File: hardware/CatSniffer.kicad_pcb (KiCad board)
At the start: 4 copper layers, 81 x 20 mm, 100 parts, among them J1 Antenna, J3 Conn_01x06_Female, P1 USB_C_Plug_USB2.0, SW1 SW, U1 AP2112K-3.3, U2 RFSW8006QTR7, U3 RP2040, U4 0900PC15A0036, U5 0900FM15D0039, U6 PE42421, U7 SX1262IMLTRT, U8 CC1352P1F3RGZT, U9 W25Q16JV, Y1 48MHz, Y2 32.768kHz, Y3 32Mhz, Y4 12MHz

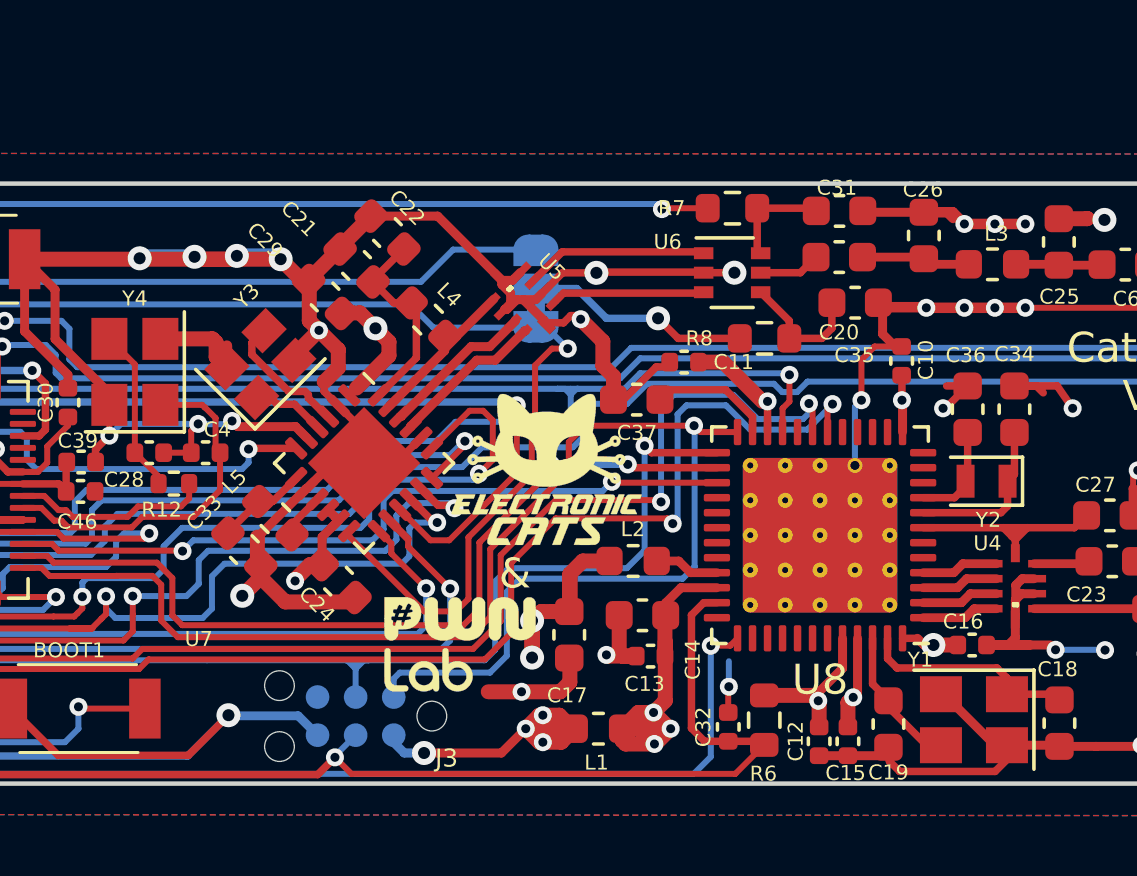
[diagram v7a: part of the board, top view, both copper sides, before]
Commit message: fix serigraphy
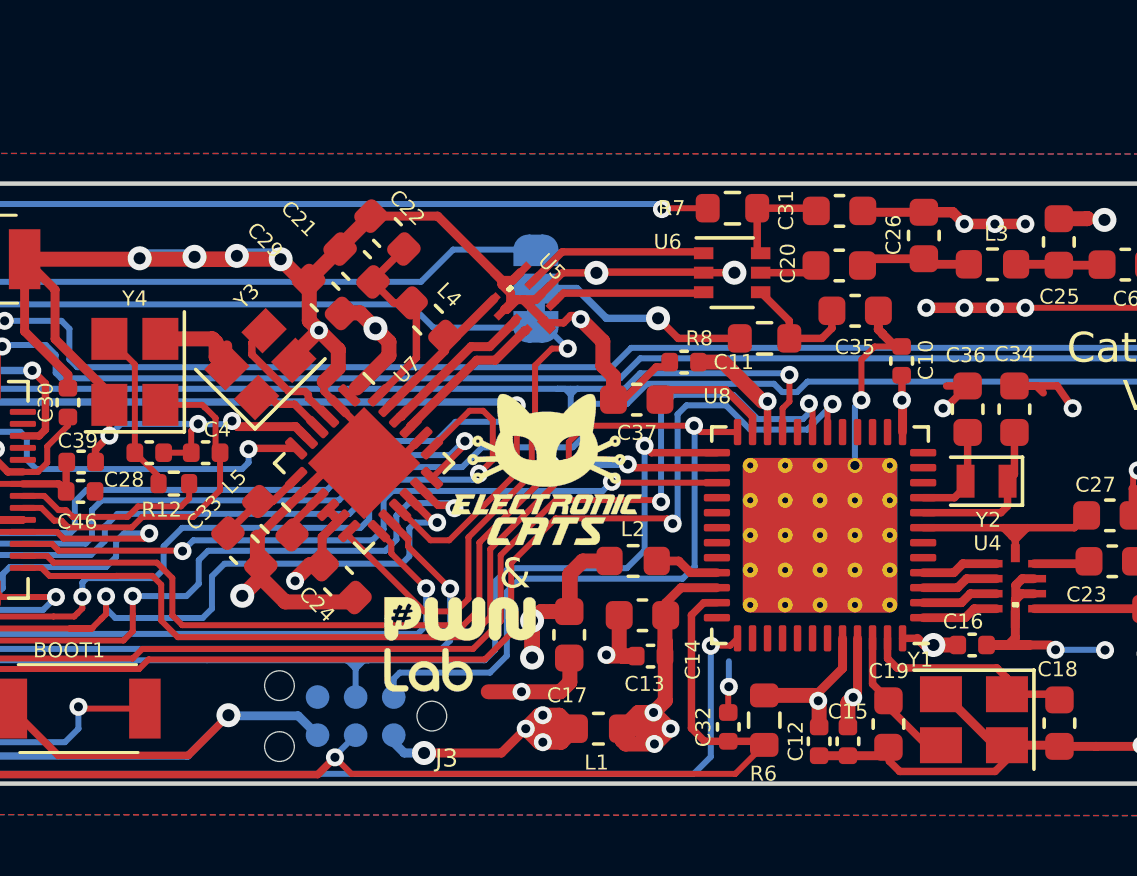
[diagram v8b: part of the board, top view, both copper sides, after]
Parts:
- moved C20 0.28 mm to (141.4, 102.7)
- moved C35 0.27 mm to (141.9, 104.2)
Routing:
- net GND: track 429.1 -> 427.3 mm
